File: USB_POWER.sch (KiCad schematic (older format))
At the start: 26 parts

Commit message: update power mark,
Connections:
- net labels added: VCC-5V, VCC-IO
- net labels removed: Vcc-5V, Vcc-io
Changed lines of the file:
@@
 $Descr A3 16535 11693
 encoding utf-8
-Sheet 12 33
+Sheet 12 34
 Title ""
 Date ""
@@
 $EndComp
 $Comp
-L taobao-components:Vcc-io #PWR?
-U 1 1 5C2AAC8D
-P 1950 950
-AR Path="/5C77255A/5C2AAC8D" Ref="#PWR?"  Part="1"
-AR Path="/5C22EE91/5C2AAC8D" Ref="#PWR?"  Part="1"
-AR Path="/5C22DA43/5C2AAC8D" Ref="#PWR?"  Part="1"
-F 0 "#PWR?" H 1950 800 50  0001 C CNN
-F 1 "Vcc-io" H 1955 1073 50  0000 C CNN
-F 2 "" H 1950 950 50  0001 C CNN
-F 3 "" H 1950 950 50  0001 C CNN
-	1    1950 950
-	1    0    0    -1
-$EndComp
-$Comp
 L taobao-r:R103,0603 R?
 U 1 1 5C2AAD60
@@
 	8300 2000 7900 2000
 Connection ~ 7900 2000
-$Comp
-L taobao-components:Vcc-5V #PWR?
-U 1 1 5C2C00C6
-P 8300 1400
-AR Path="/5C77255A/5C2C00C6" Ref="#PWR?"  Part="1"
-AR Path="/5C22EE91/5C2C00C6" Ref="#PWR?"  Part="1"
-AR Path="/5C22DA43/5C2C00C6" Ref="#PWR?"  Part="1"
-F 0 "#PWR?" H 8300 1250 50  0001 C CNN
-F 1 "Vcc-5V" H 8305 1523 50  0000 C CNN
-F 2 "" H 8300 1400 50  0001 C CNN
-F 3 "" H 8300 1400 50  0001 C CNN
-	1    8300 1400
-	1    0    0    -1
-$EndComp
 Wire Wire Line
 	8300 1400 8300 1500
@@
 $EndComp
 $Comp
-L taobao-components:Vcc-5V #PWR?
-U 1 1 5C2C7E3C
-P 3150 5500
-AR Path="/5C77255A/5C2C7E3C" Ref="#PWR?"  Part="1"
-AR Path="/5C22EE91/5C2C7E3C" Ref="#PWR?"  Part="1"
-AR Path="/5C22DA43/5C2C7E3C" Ref="#PWR?"  Part="1"
-F 0 "#PWR?" H 3150 5350 50  0001 C CNN
-F 1 "Vcc-5V" H 3155 5623 50  0000 C CNN
-F 2 "" H 3150 5500 50  0001 C CNN
-F 3 "" H 3150 5500 50  0001 C CNN
-	1    3150 5500
-	1    0    0    -1
-$EndComp
-$Comp
 L taobao-components:HOST-VBUS #PWR?
 U 1 1 5C2CBE64
@@
 Wire Wire Line
 	2450 12150 3400 12150
+$Comp
+L taobao-components:VCC-IO #PWR?
+U 1 1 5C7D8724
+P 1950 950
+F 0 "#PWR?" H 1950 800 50  0001 C CNN
+F 1 "VCC-IO" H 2000 1100 50  0000 C CNN
+F 2 "" H 1950 950 50  0001 C CNN
+F 3 "" H 1950 950 50  0001 C CNN
+	1    1950 950
+	1    0    0    -1
+$EndComp
+$Comp
+L taobao-components:VCC-5V #PWR?
+U 1 1 5C7DB996
+P 8300 1400
+F 0 "#PWR?" H 8300 1250 50  0001 C CNN
+F 1 "VCC-5V" H 8350 1550 50  0000 C CNN
+F 2 "" H 8300 1400 50  0001 C CNN
+F 3 "" H 8300 1400 50  0001 C CNN
+	1    8300 1400
+	1    0    0    -1
+$EndComp
+$Comp
+L taobao-components:VCC-5V #PWR?
+U 1 1 5C7DBA7D
+P 3150 5500
+F 0 "#PWR?" H 3150 5350 50  0001 C CNN
+F 1 "VCC-5V" H 3200 5650 50  0000 C CNN
+F 2 "" H 3150 5500 50  0001 C CNN
+F 3 "" H 3150 5500 50  0001 C CNN
+	1    3150 5500
+	1    0    0    -1
+$EndComp
 $EndSCHEMATC

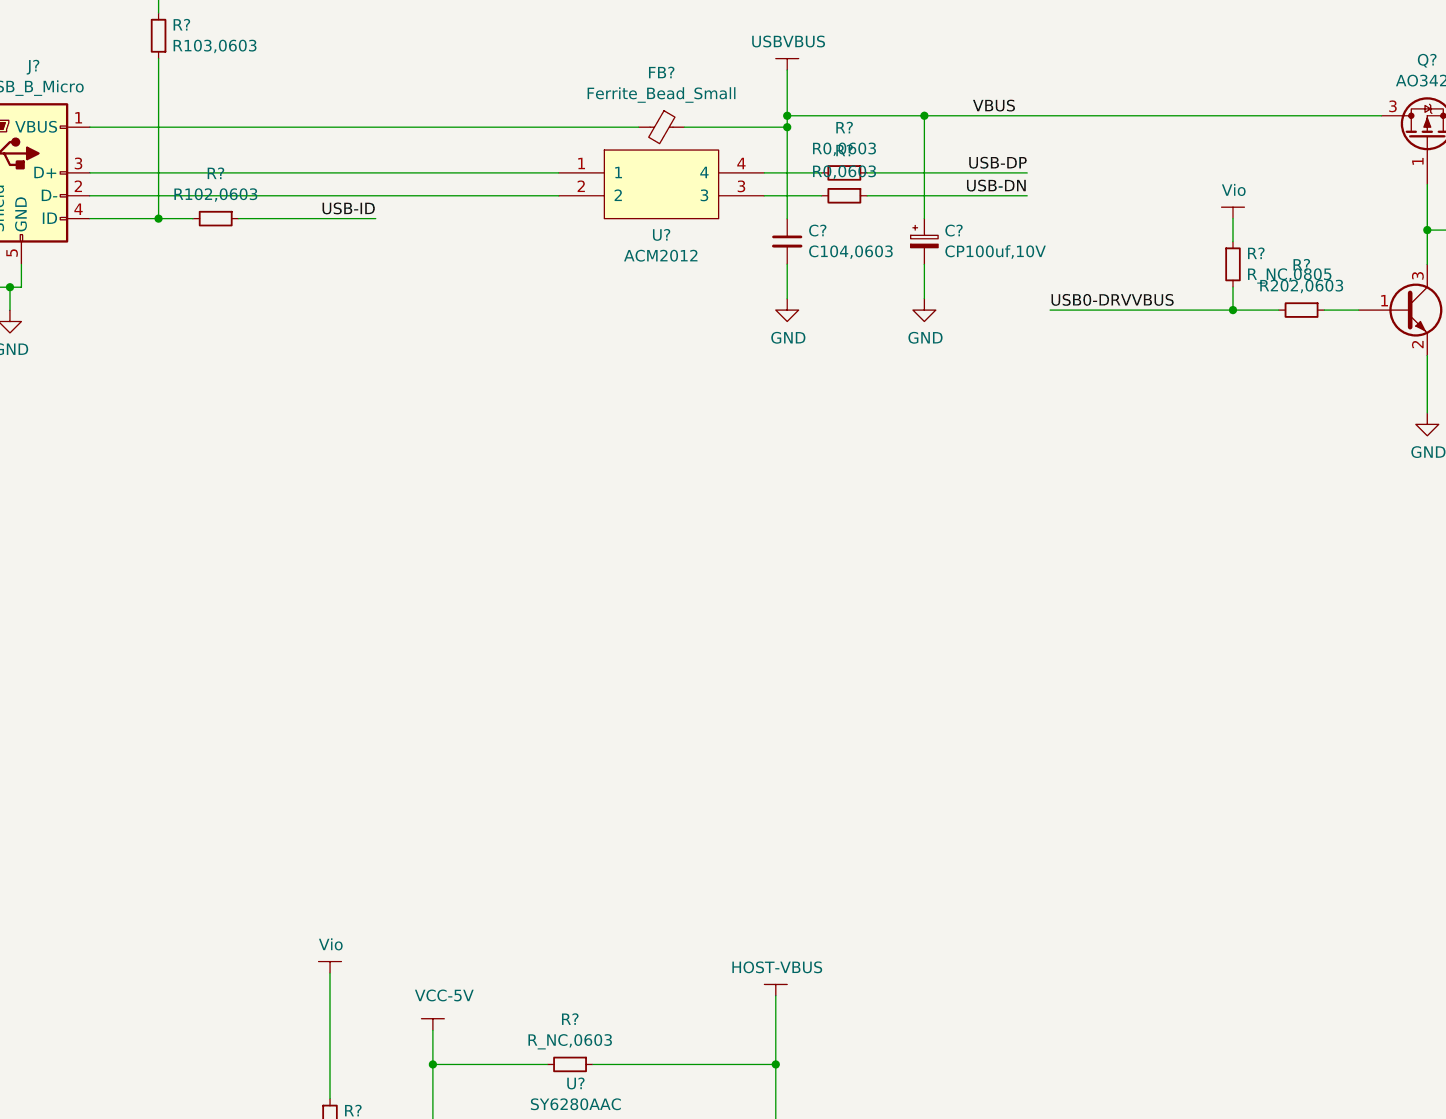
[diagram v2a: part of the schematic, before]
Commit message: update Vio -> VCC-IO,
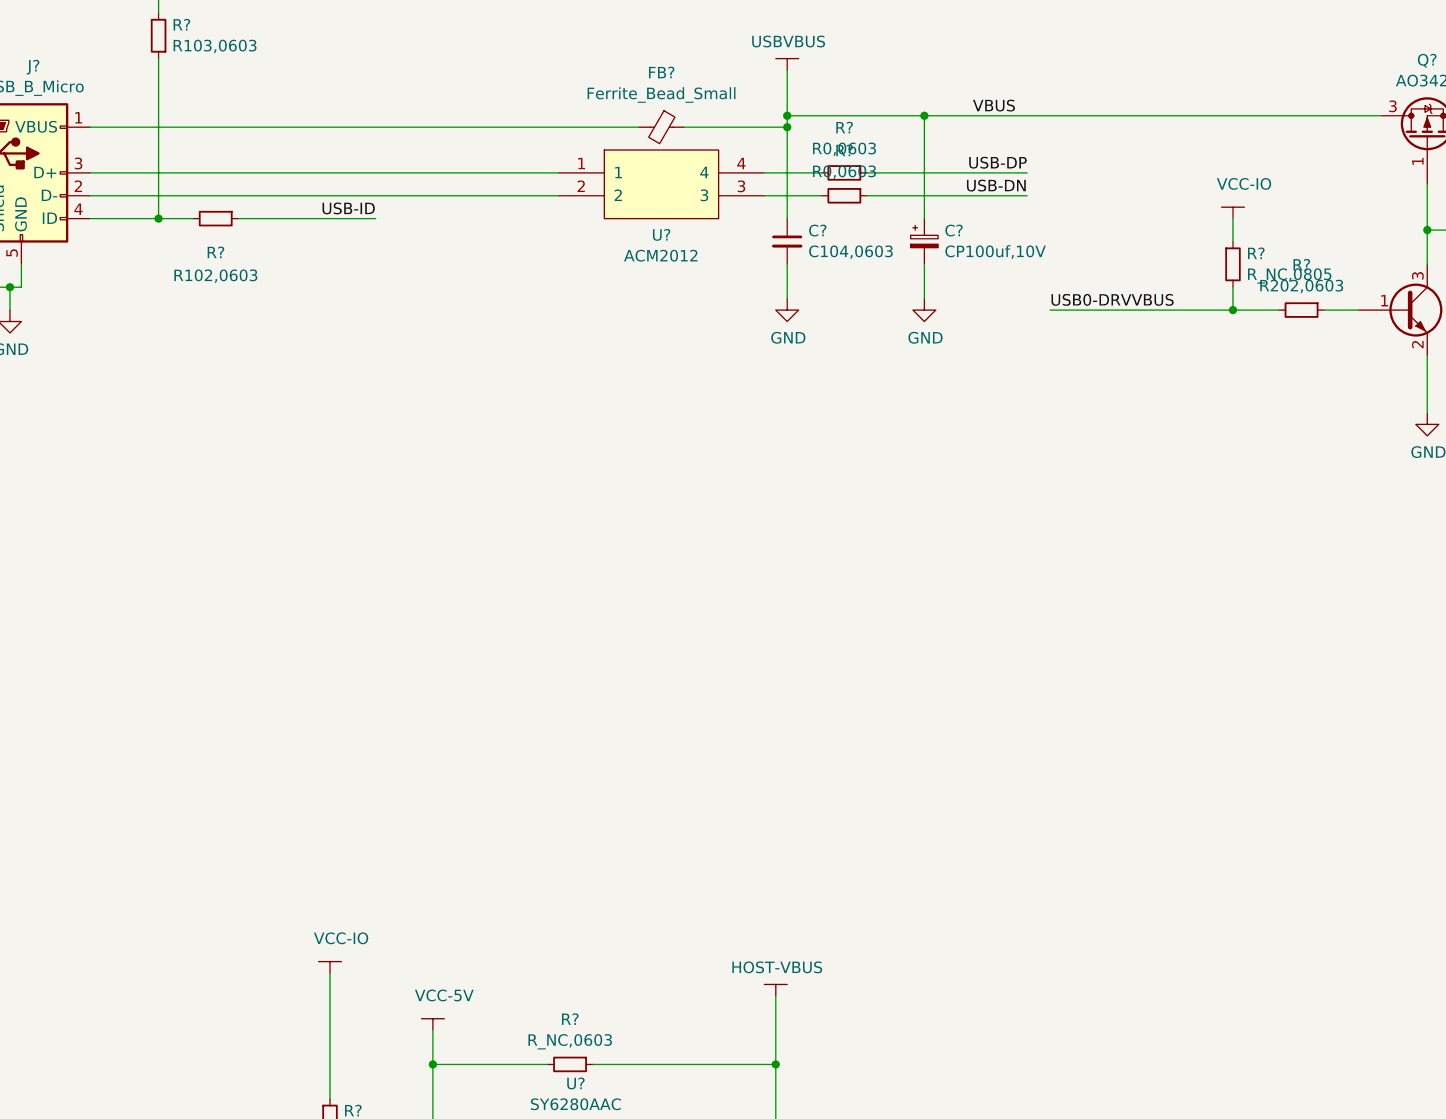
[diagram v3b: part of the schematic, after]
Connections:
- net Vio is gone; now on net VCC-IO: R?.1, R?.1
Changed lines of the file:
@@
 $EndComp
 $Comp
-L taobao-components:Vio #PWR?
-U 1 1 5C2AFCC0
-P 6650 1950
-AR Path="/5C77255A/5C2AFCC0" Ref="#PWR?"  Part="1"
-AR Path="/5C22EE91/5C2AFCC0" Ref="#PWR?"  Part="1"
-AR Path="/5C22DA43/5C2AFCC0" Ref="#PWR?"  Part="1"
-F 0 "#PWR?" H 6650 1800 50  0001 C CNN
-F 1 "Vio" H 6655 2073 50  0000 C CNN
-F 2 "" H 6650 1950 50  0001 C CNN
-F 3 "" H 6650 1950 50  0001 C CNN
-	1    6650 1950
-	1    0    0    -1
-$EndComp
-$Comp
 L taobao-components:R_NC,0805 R?
 U 1 1 5C2BDE1D
@@
 AR Path="/5C22EE91/5C2C0789" Ref="R?"  Part="1"
 AR Path="/5C22DA43/5C2C0789" Ref="R?"  Part="1"
-F 0 "R?" V 2004 1950 50  0000 C CNN
-F 1 "R102,0603" V 2095 1950 50  0000 C CNN
+F 0 "R?" V 2350 1950 50  0000 C CNN
+F 1 "R102,0603" V 2450 1950 50  0000 C CNN
 F 2 "Resistor_SMD:R_0603_1608Metric_Pad1.05x0.95mm_HandSolder" H 2200 1950 50  0001 C CNN
 F 3 "~" H 2200 1950 50  0001 C CNN
@@
 $EndBitmap
 $Comp
-L taobao-components:Vio #PWR?
-U 1 1 5C2C7D65
-P 2700 5250
-AR Path="/5C77255A/5C2C7D65" Ref="#PWR?"  Part="1"
-AR Path="/5C22EE91/5C2C7D65" Ref="#PWR?"  Part="1"
-AR Path="/5C22DA43/5C2C7D65" Ref="#PWR?"  Part="1"
-F 0 "#PWR?" H 2700 5100 50  0001 C CNN
-F 1 "Vio" H 2705 5373 50  0000 C CNN
-F 2 "" H 2700 5250 50  0001 C CNN
-F 3 "" H 2700 5250 50  0001 C CNN
-	1    2700 5250
-	1    0    0    -1
-$EndComp
-$Comp
 L taobao-components:HOST-VBUS #PWR?
 U 1 1 5C2CBE64
@@
 	1    0    0    -1
 $EndComp
+$Comp
+L taobao-components:VCC-IO #PWR?
+U 1 1 5C7DEA34
+P 2700 5250
+F 0 "#PWR?" H 2700 5100 50  0001 C CNN
+F 1 "VCC-IO" H 2750 5400 50  0000 C CNN
+F 2 "" H 2700 5250 50  0001 C CNN
+F 3 "" H 2700 5250 50  0001 C CNN
+	1    2700 5250
+	1    0    0    -1
+$EndComp
+$Comp
+L taobao-components:VCC-IO #PWR?
+U 1 1 5C7DEB72
+P 6650 1950
+F 0 "#PWR?" H 6650 1800 50  0001 C CNN
+F 1 "VCC-IO" H 6700 2100 50  0000 C CNN
+F 2 "" H 6650 1950 50  0001 C CNN
+F 3 "" H 6650 1950 50  0001 C CNN
+	1    6650 1950
+	1    0    0    -1
+$EndComp

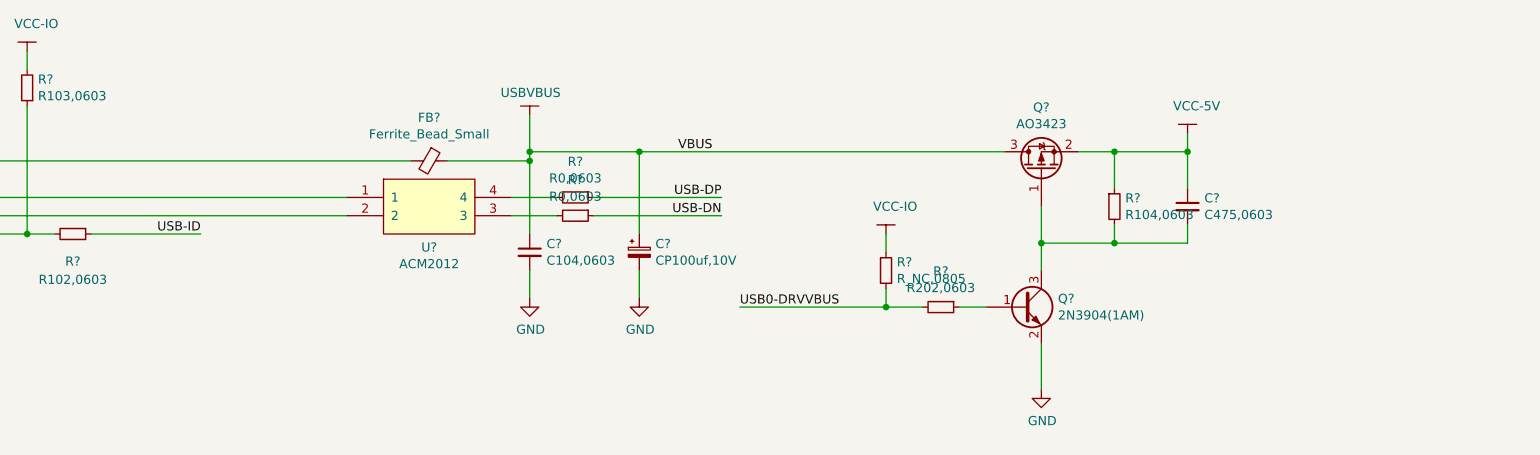
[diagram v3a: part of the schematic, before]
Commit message: update USB schematic,
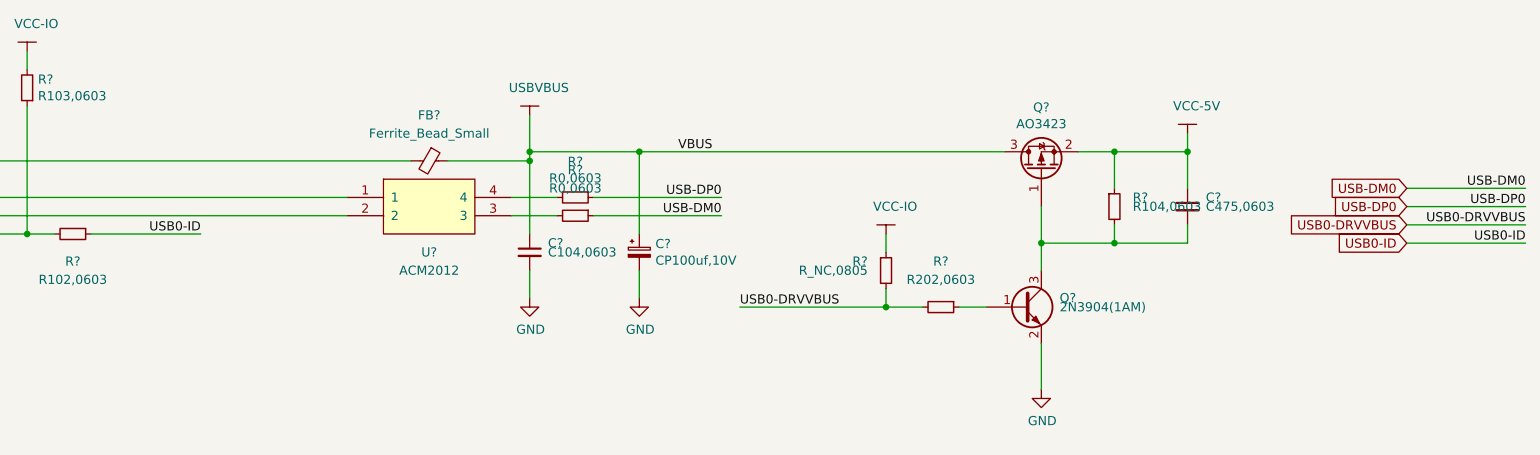
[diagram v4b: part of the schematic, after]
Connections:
- net USB-DN renamed USB-DM0
- net USB-DP renamed USB-DP0
- net USB-ID renamed USB0-ID
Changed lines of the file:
@@
 AR Path="/5C22EE91/5C2AA98F" Ref="U?"  Part="1"
 AR Path="/5C22DA43/5C2AA98F" Ref="U?"  Part="1"
-F 0 "U?" H 4150 1577 50  0000 C CNN
-F 1 "ACM2012" H 4150 1486 50  0000 C CNN
+F 0 "U?" H 4150 1550 50  0000 C CNN
+F 1 "ACM2012" H 4150 1450 50  0000 C CNN
 F 2 "" H 4150 1800 50  0001 C CNN
 F 3 "" H 4150 1800 50  0001 C CNN
@@
 AR Path="/5C22EE91/5C2AAB88" Ref="FB?"  Part="1"
 AR Path="/5C22DA43/5C2AAB88" Ref="FB?"  Part="1"
-F 0 "FB?" V 3913 1550 50  0000 C CNN
-F 1 "Ferrite_Bead_Small" V 4004 1550 50  0000 C CNN
+F 0 "FB?" V 3900 1550 50  0000 C CNN
+F 1 "Ferrite_Bead_Small" V 4000 1550 50  0000 C CNN
 F 2 "" V 4080 1550 50  0001 C CNN
 F 3 "~" H 4150 1550 50  0001 C CNN
@@
 AR Path="/5C22DA43/5C2AE79C" Ref="#PWR?"  Part="1"
 F 0 "#PWR?" H 4700 1150 50  0001 C CNN
-F 1 "USBVBUS" H 4705 1423 50  0000 C CNN
+F 1 "USBVBUS" H 4750 1450 50  0000 C CNN
 F 2 "" H 4700 1300 50  0001 C CNN
 F 3 "" H 4700 1300 50  0001 C CNN
@@
 AR Path="/5C22EE91/5C2AE8CB" Ref="R?"  Part="1"
 AR Path="/5C22DA43/5C2AE8CB" Ref="R?"  Part="1"
-F 0 "R?" V 4754 1850 50  0000 C CNN
-F 1 "R0,0603" V 4845 1850 50  0000 C CNN
+F 0 "R?" V 4700 1850 50  0000 C CNN
+F 1 "R0,0603" V 4800 1850 50  0000 C CNN
 F 2 "Resistor_SMD:R_0603_1608Metric_Pad1.05x0.95mm_HandSolder" H 4950 1850 50  0001 C CNN
 F 3 "~" H 4950 1850 50  0001 C CNN
@@
 	4850 1850 4600 1850
 Text Label 5750 1850 2    50   ~ 0
-USB-DN
+USB-DM0
 Text Label 5750 1750 2    50   ~ 0
-USB-DP
+USB-DP0
 Wire Wire Line
 	5750 1750 5050 1750
@@
 AR Path="/5C22EE91/5C2AEBE0" Ref="C?"  Part="1"
 AR Path="/5C22DA43/5C2AEBE0" Ref="C?"  Part="1"
-F 0 "C?" H 4792 2096 50  0000 L CNN
-F 1 "C104,0603" H 4792 2005 50  0000 L CNN
+F 0 "C?" H 4800 2100 50  0000 L CNN
+F 1 "C104,0603" H 4800 2050 50  0000 L CNN
 F 2 "Capacitor_SMD:C_0603_1608Metric_Pad1.05x0.95mm_HandSolder" H 4700 2050 50  0001 C CNN
 F 3 "~" H 4700 2050 50  0001 C CNN
@@
 AR Path="/5C22EE91/5C2AF9E3" Ref="Q?"  Part="1"
 AR Path="/5C22DA43/5C2AF9E3" Ref="Q?"  Part="1"
-F 0 "Q?" H 7591 2396 50  0000 L CNN
-F 1 "2N3904(1AM)" H 7591 2305 50  0000 L CNN
+F 0 "Q?" H 7600 2400 50  0000 L CNN
+F 1 "2N3904(1AM)" H 7600 2350 50  0000 L CNN
 F 2 "Package_TO_SOT_THT:TO-92_Inline" H 7600 2275 50  0001 L CIN
 F 3 "" H 7400 2350 50  0001 L CNN
@@
 AR Path="/5C22EE91/5C2BDE1D" Ref="R?"  Part="1"
 AR Path="/5C22DA43/5C2BDE1D" Ref="R?"  Part="1"
-F 0 "R?" H 6709 2196 50  0000 L CNN
-F 1 "R_NC,0805" H 6709 2105 50  0000 L CNN
+F 0 "R?" H 6550 2200 50  0000 R CNN
+F 1 "R_NC,0805" H 6550 2150 50  0000 R CNN
 F 2 "Resistor_SMD:R_0805_2012Metric_Pad1.15x1.40mm_HandSolder" H 6650 2150 50  0001 C CNN
 F 3 "~" H 6650 2150 50  0001 C CNN
@@
 AR Path="/5C22EE91/5C2BE39F" Ref="R?"  Part="1"
 AR Path="/5C22DA43/5C2BE39F" Ref="R?"  Part="1"
-F 0 "R?" V 6754 2350 50  0000 C CNN
-F 1 "R202,0603" V 6845 2350 50  0000 C CNN
+F 0 "R?" V 6700 2350 50  0000 C CNN
+F 1 "R202,0603" V 6800 2350 50  0000 C CNN
 F 2 "Resistor_SMD:R_0603_1608Metric_Pad1.05x0.95mm_HandSolder" H 6950 2350 50  0001 C CNN
 F 3 "~" H 6950 2350 50  0001 C CNN
@@
 AR Path="/5C22EE91/5C2BEF72" Ref="R?"  Part="1"
 AR Path="/5C22DA43/5C2BEF72" Ref="R?"  Part="1"
-F 0 "R?" H 7959 1846 50  0000 L CNN
-F 1 "R104,0603" H 7959 1755 50  0000 L CNN
+F 0 "R?" H 8000 1850 50  0000 L CNN
+F 1 "R104,0603" H 8000 1800 50  0000 L CNN
 F 2 "Resistor_SMD:R_0603_1608Metric_Pad1.05x0.95mm_HandSolder" H 7900 1800 50  0001 C CNN
 F 3 "~" H 7900 1800 50  0001 C CNN
@@
 AR Path="/5C22EE91/5C2BF09A" Ref="C?"  Part="1"
 AR Path="/5C22DA43/5C2BF09A" Ref="C?"  Part="1"
-F 0 "C?" H 8392 1846 50  0000 L CNN
-F 1 "C475,0603" H 8392 1755 50  0000 L CNN
+F 0 "C?" H 8400 1850 50  0000 L CNN
+F 1 "C475,0603" H 8400 1800 50  0000 L CNN
 F 2 "Capacitor_SMD:C_0603_1608Metric_Pad1.05x0.95mm_HandSolder" H 8300 1800 50  0001 C CNN
 F 3 "~" H 8300 1800 50  0001 C CNN
@@
 	1650 1950 1950 1950
 Text Label 2900 1950 2    50   ~ 0
-USB-ID
+USB0-ID
 Wire Wire Line
 	2300 1950 2900 1950
@@
 	1    0    0    -1
 $EndComp
+Text GLabel 9500 1700 0    50   Input ~ 0
+USB-DM0
+Text Label 10150 1700 2    50   ~ 0
+USB-DM0
+Wire Wire Line
+	10150 1700 9500 1700
+Text GLabel 9500 1800 0    50   Input ~ 0
+USB-DP0
+Text Label 10150 1800 2    50   ~ 0
+USB-DP0
+Wire Wire Line
+	10150 1800 9500 1800
+Text GLabel 9500 1900 0    50   Input ~ 0
+USB0-DRVVBUS
+Text Label 10150 1900 2    50   ~ 0
+USB0-DRVVBUS
+Wire Wire Line
+	10150 1900 9500 1900
+Text GLabel 9500 2000 0    50   Input ~ 0
+USB0-ID
+Text Label 10150 2000 2    50   ~ 0
+USB0-ID
+Wire Wire Line
+	10150 2000 9500 2000
 $EndSCHEMATC
